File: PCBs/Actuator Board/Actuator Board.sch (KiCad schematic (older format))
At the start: 14 parts

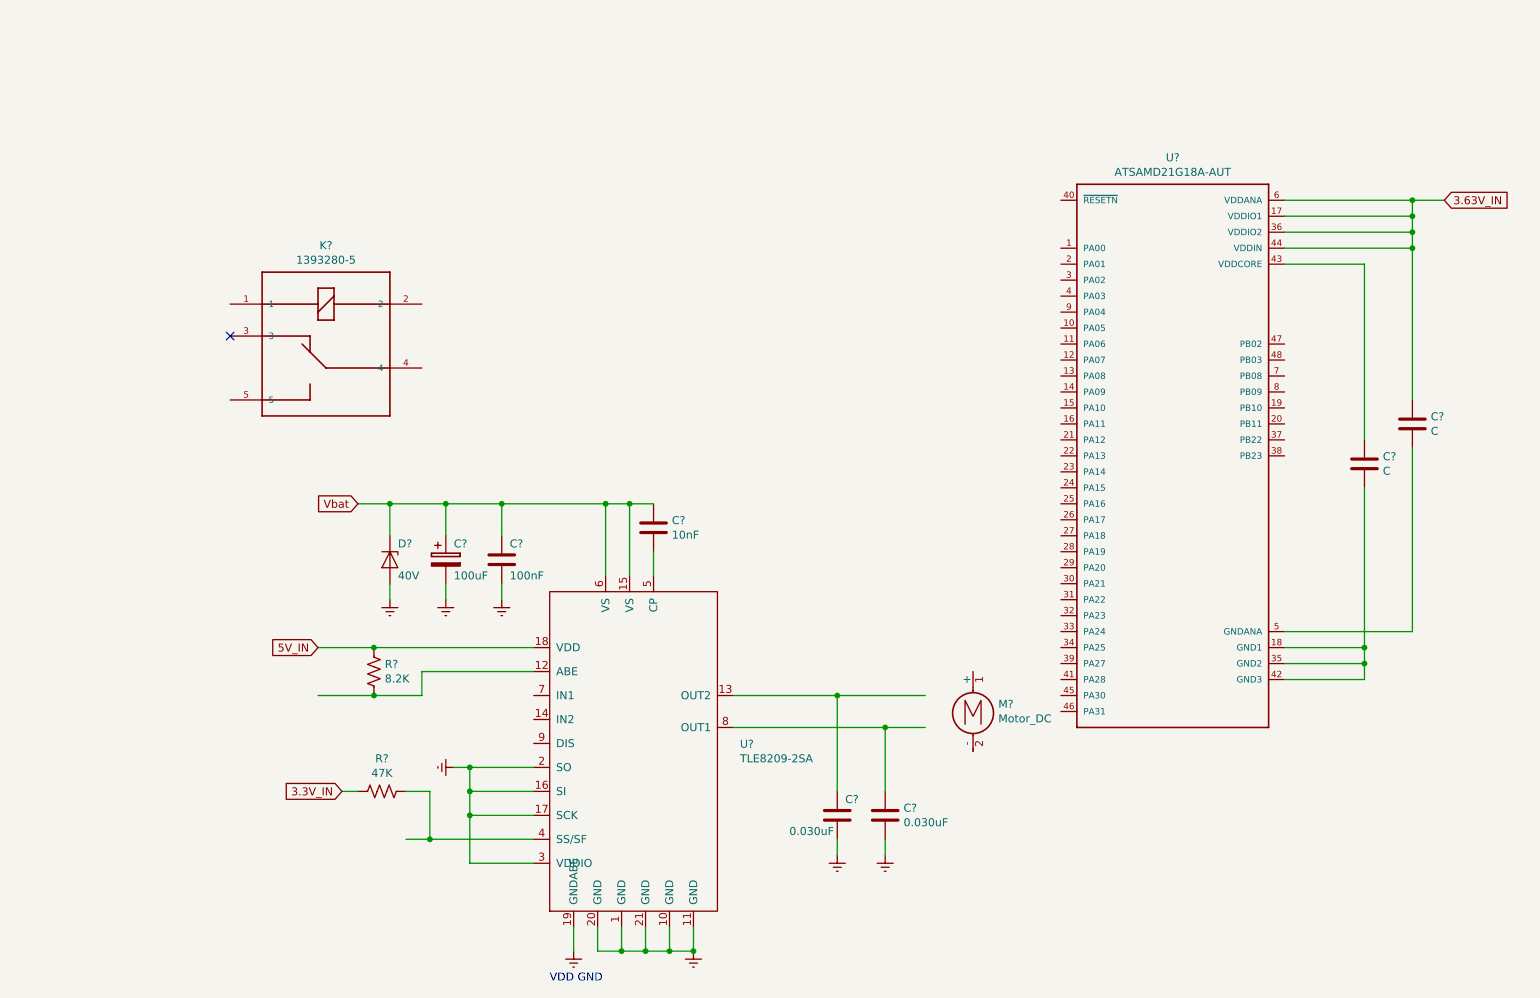
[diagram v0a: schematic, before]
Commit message: Started Relay
finish relay values
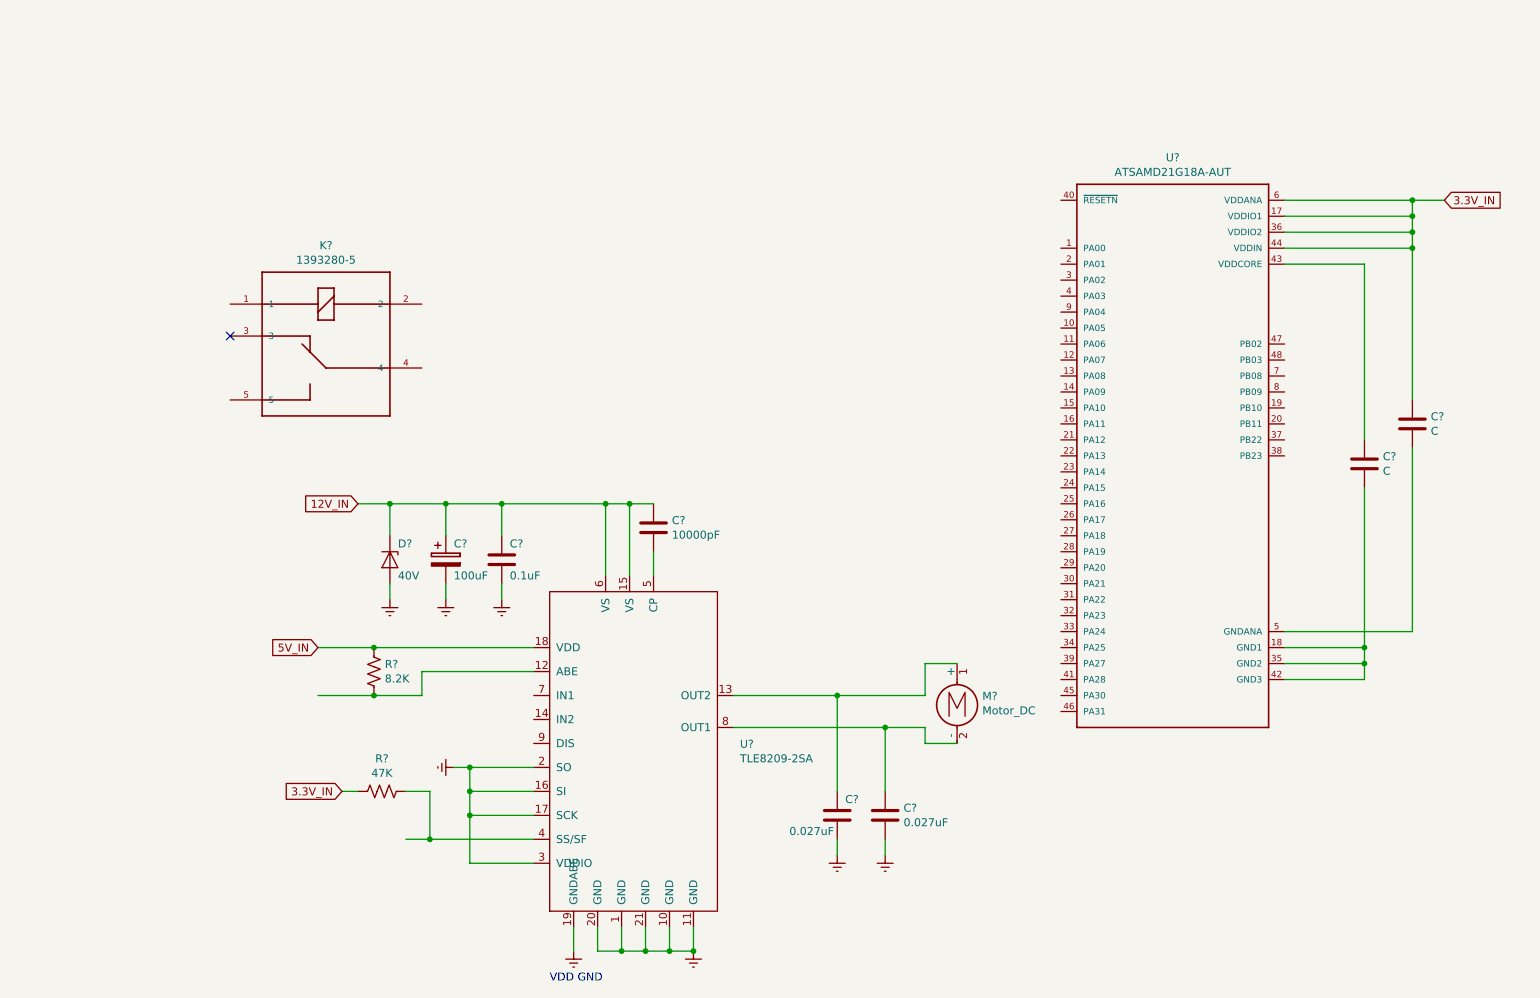
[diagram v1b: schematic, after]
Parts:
- C?: value 10nF -> 10000pF
- C?: value 100nF -> 0.1uF
- C? (x2): value 0.030uF -> 0.027uF
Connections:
- net labels added: 12V_IN
- net labels removed: 3.63V_IN, Vbat
- wire segments 71 -> 75
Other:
- moved on the sheet: M?
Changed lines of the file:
@@
 Connection ~ 10000 4550
 Text GLabel 10500 1650 2    50   Input ~ 0
-3.63V_IN
+3.3V_IN
 $Comp
 L Device:C C?
@@
 P 5550 3700
 F 0 "C?" H 5665 3746 50  0000 L CNN
-F 1 "10nF" H 5665 3655 50  0000 L CNN
+F 1 "10000pF" H 5665 3655 50  0000 L CNN
 F 2 "" H 5588 3550 50  0001 C CNN
 F 3 "~" H 5550 3700 50  0001 C CNN
@@
 P 4600 3900
 F 0 "C?" H 4650 4000 50  0000 L CNN
-F 1 "100nF" H 4650 3800 50  0000 L CNN
+F 1 "0.1uF" H 4650 3800 50  0000 L CNN
 F 2 "" H 4638 3750 50  0001 C CNN
 F 3 "~" H 4600 3900 50  0001 C CNN
@@
 Wire Wire Line
 	3900 3550 4250 3550
-Text GLabel 3700 3550 0    50   Input ~ 0
-Vbat
 $Comp
 L TLE8209-2SA:TLE8209-2SA U?
@@
 P 6700 5500
 F 0 "C?" H 6750 5600 50  0000 L CNN
-F 1 "0.030uF" H 6400 5400 50  0000 L CNN
+F 1 "0.027uF" H 6400 5400 50  0000 L CNN
 F 2 "" H 6738 5350 50  0001 C CNN
 F 3 "~" H 6700 5500 50  0001 C CNN
@@
 P 7000 5500
 F 0 "C?" H 7115 5546 50  0000 L CNN
-F 1 "0.030uF" H 7115 5455 50  0000 L CNN
+F 1 "0.027uF" H 7115 5455 50  0000 L CNN
 F 2 "" H 7038 5350 50  0001 C CNN
 F 3 "~" H 7000 5500 50  0001 C CNN
@@
 L Motor:Motor_DC M?
 U 1 1 5BDF467F
-P 7550 4800
-F 0 "M?" H 7708 4796 50  0000 L CNN
-F 1 "Motor_DC" H 7708 4705 50  0000 L CNN
-F 2 "" H 7550 4710 50  0001 C CNN
-F 3 "~" H 7550 4710 50  0001 C CNN
-	1    7550 4800
-	1    0    0    -1
-$EndComp
+P 7450 4750
+F 0 "M?" H 7608 4746 50  0000 L CNN
+F 1 "Motor_DC" H 7608 4655 50  0000 L CNN
+F 2 "" H 7450 4660 50  0001 C CNN
+F 3 "~" H 7450 4660 50  0001 C CNN
+	1    7450 4750
+	1    0    0    -1
+$EndComp
+Text GLabel 3700 3550 0    50   Input ~ 0
+12V_IN
+Wire Wire Line
+	7250 4750 7250 4550
+Wire Wire Line
+	7250 4550 7450 4550
+Wire Wire Line
+	7250 4950 7250 5050
+Wire Wire Line
+	7250 5050 7450 5050
 $EndSCHEMATC

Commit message: started relay
this actualy has the relay started
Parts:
- added D?: LED, symbol Device:LED
- added D?: D, symbol Device:D
- added Q?: BC547, Package_TO_SOT_THT:TO-92_Inline, symbol Transistor_BJT:BC547
- added R?: 590, symbol Device:R_US
- added R? (x2): R_US, symbol Device:R_US
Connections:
- net labels added: +12V, +3.3V, UC_IN
- wire segments 75 -> 96
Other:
- note added: "+"
- note added: "-\n"
- moved on the sheet: K?
